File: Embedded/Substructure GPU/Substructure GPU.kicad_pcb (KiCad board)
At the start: 4 copper layers, 50 x 35 mm, 35 parts, among them J1 10171746-00021LF, J11 Substructure Power, J13 MicroSD, J2 HUB75 Right, J3 Display Power, J4 HUB75 Left, SW2 RST, U2 74HC245D_653, U3 74HC245D_653, U5 Substructure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

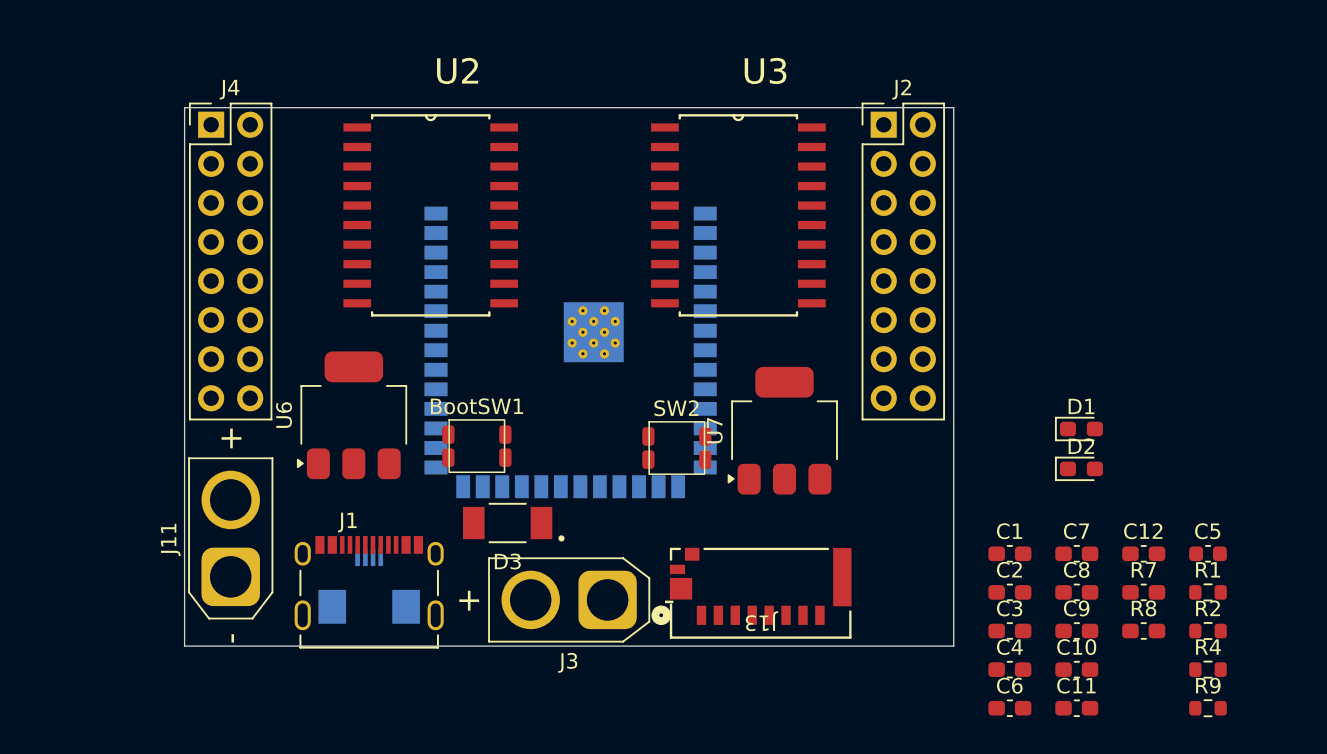
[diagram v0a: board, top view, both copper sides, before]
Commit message: Modified Board size
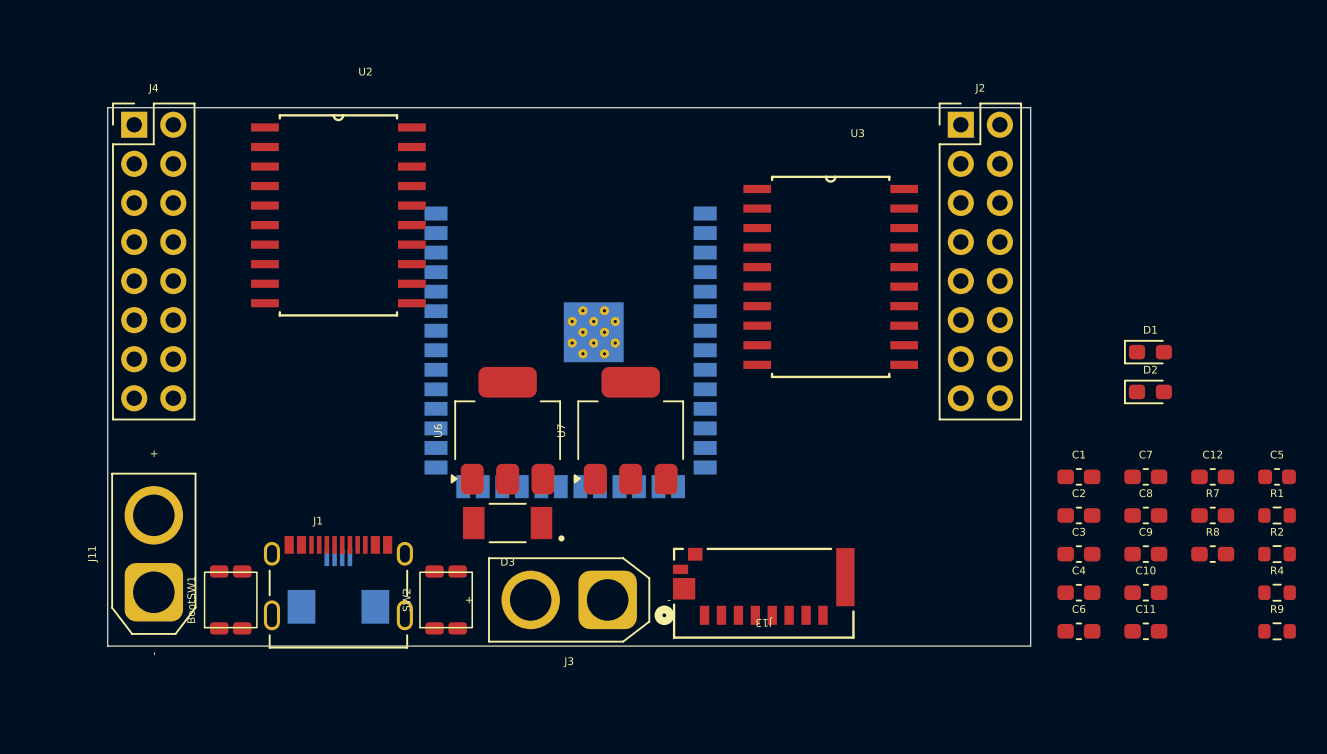
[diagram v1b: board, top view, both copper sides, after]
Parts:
- moved BootSW1 18.9 mm to (73.0, 72.0), turned to 90 degrees
- moved SW2 18.0 mm to (87.0, 72.0), turned to 90 degrees
- moved U6 10.0 mm to (91.0, 61.0)
- moved U7 10.0 mm to (99.0, 61.0)
- moved U3 7.21 mm to (112.0, 51.0)
- moved C10 6.72 mm to (132.5, 71.5)
- moved C11 6.72 mm to (132.5, 74.0)
- moved C12 6.72 mm to (136.8, 64.0)
- moved C5 6.72 mm to (141.0, 64.0)
- moved C7 6.72 mm to (132.5, 64.0)
- moved C8 6.72 mm to (132.5, 66.5)
- moved C9 6.72 mm to (132.5, 69.0)
- moved R1 6.72 mm to (141.0, 66.5)
- moved R2 6.72 mm to (141.0, 69.0)
- moved R4 6.72 mm to (141.0, 71.5)
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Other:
- board size 50 x 35 mm -> 60 x 35 mm

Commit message: Added Component placement for driver components
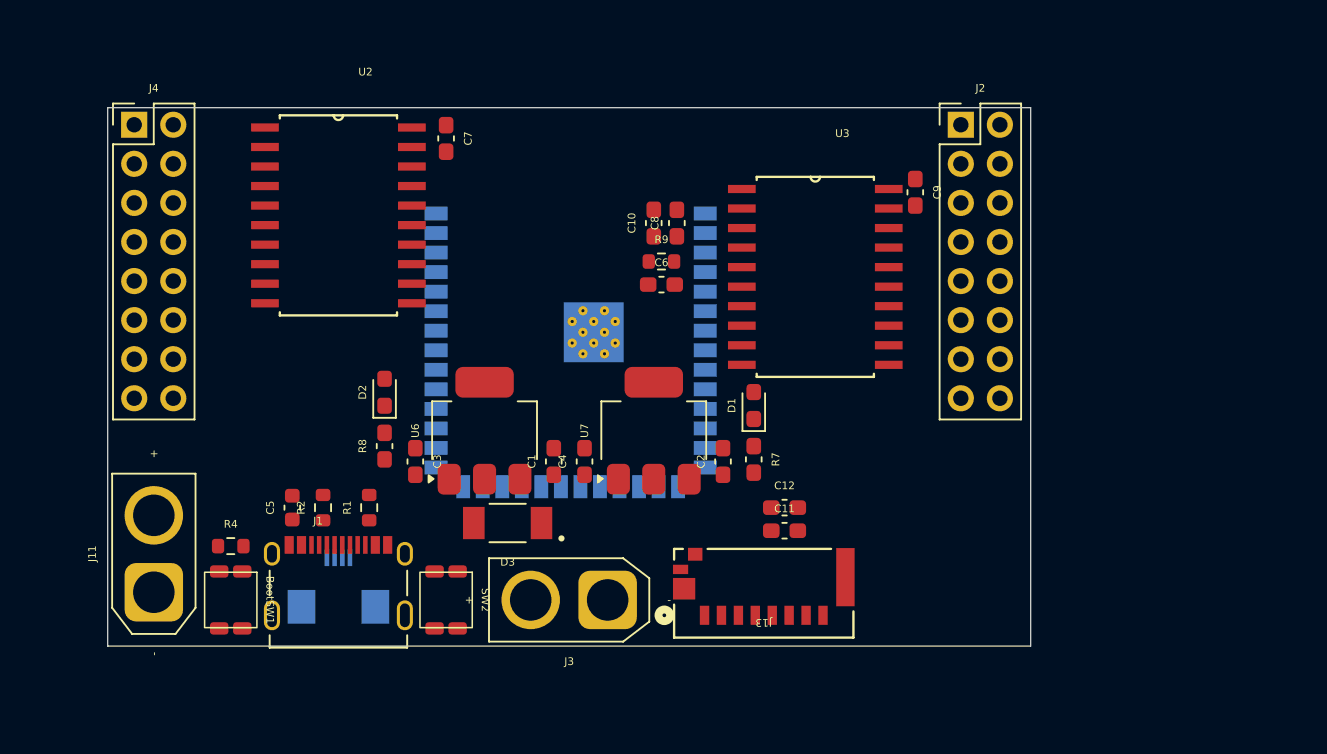
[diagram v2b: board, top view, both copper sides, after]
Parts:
- moved R4 68.1 mm to (73.0, 68.5)
- moved C5 64.0 mm to (77.0, 66.0), turned to 90 degrees
- moved R2 62.1 mm to (79.0, 66.0), turned to 90 degrees
- moved R1 59.0 mm to (82.0, 66.0), turned to 90 degrees
- moved R8 54.3 mm to (83.0, 62.0), turned to 90 degrees
- moved C7 50.5 mm to (87.0, 42.0), turned to -90 degrees
- moved D2 49.8 mm to (83.0, 58.5), turned to 90 degrees
- moved R9 46.7 mm to (101.0, 50.0)
- moved C3 43.6 mm to (85.0, 63.0), turned to -90 degrees
- moved C10 40.0 mm to (100.5, 47.5), turned to 90 degrees
- moved C8 35.9 mm to (102.0, 47.5), turned to 90 degrees
- moved C6 35.3 mm to (101.0, 51.5)
- moved C1 34.2 mm to (94.0, 63.0), turned to 90 degrees
- moved C4 33.3 mm to (96.0, 63.0), turned to 90 degrees
- moved R7 30.1 mm to (107.0, 62.9), turned to -90 degrees
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
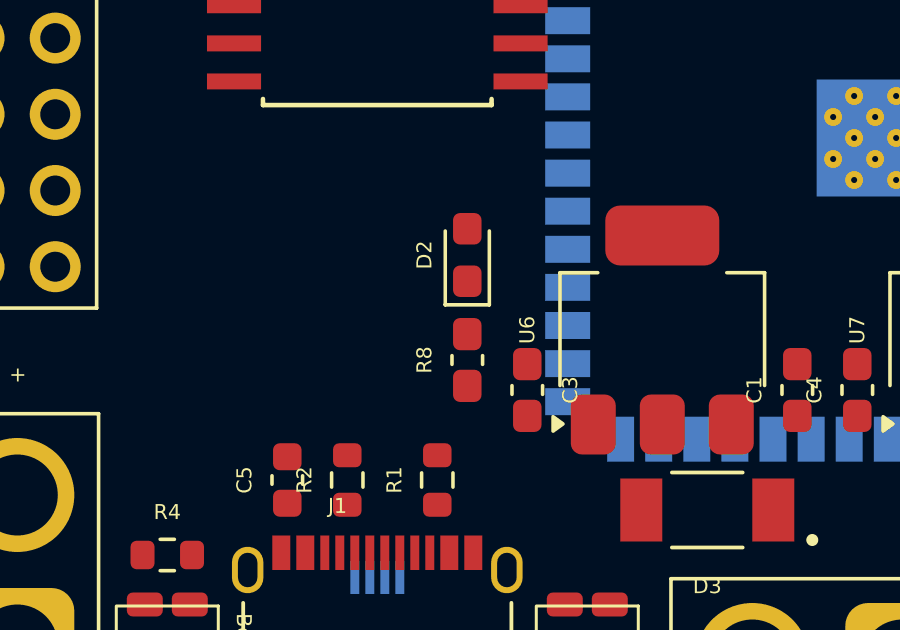
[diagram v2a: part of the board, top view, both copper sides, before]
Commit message: Added Pins to route in schematic
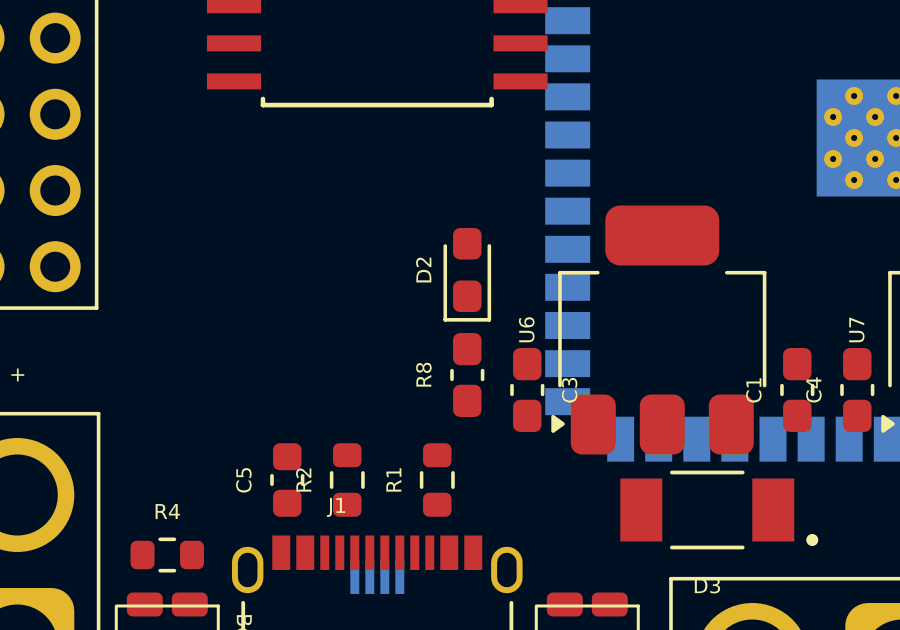
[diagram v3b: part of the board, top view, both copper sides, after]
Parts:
- moved D2 0.50 mm to (83.0, 59.0)
- moved R8 0.50 mm to (83.0, 62.5)
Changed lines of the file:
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@@
 	(footprint "Diode_SMD:D_0603_1608Metric_Pad1.05x0.95mm_HandSolder"
 		(layer "F.Cu")
-		(at 83 58.5 90)
+		(at 83 59 90)
 		(descr "Diode SMD 0603 (1608 Metric), square (rectangular) end terminal, IPC-7351 nominal, (Body size source: http://www.tortai-tech.com/upload/download/2011102023233369053.pdf), generated with kicad-footprint-generator")
 		(tags "diode handsolder")
@@
 	(footprint "Capacitor_SMD:C_0603_1608Metric_Pad1.08x0.95mm_HandSolder"
 		(layer "F.Cu")
-		(at 83 62 90)
+		(at 83 62.5 90)
 		(descr "Capacitor SMD 0603 (1608 Metric), square (rectangular) end terminal, IPC-7351 nominal with elongated pad for handsoldering. (Body size source: IPC-SM-782 page 76, https://www.pcb-3d.com/wordpress/wp-content/uploads/ipc-sm-782a_amendment_1_and_2.pdf), generated with kicad-footprint-generator")
 		(tags "capacitor handsolder")

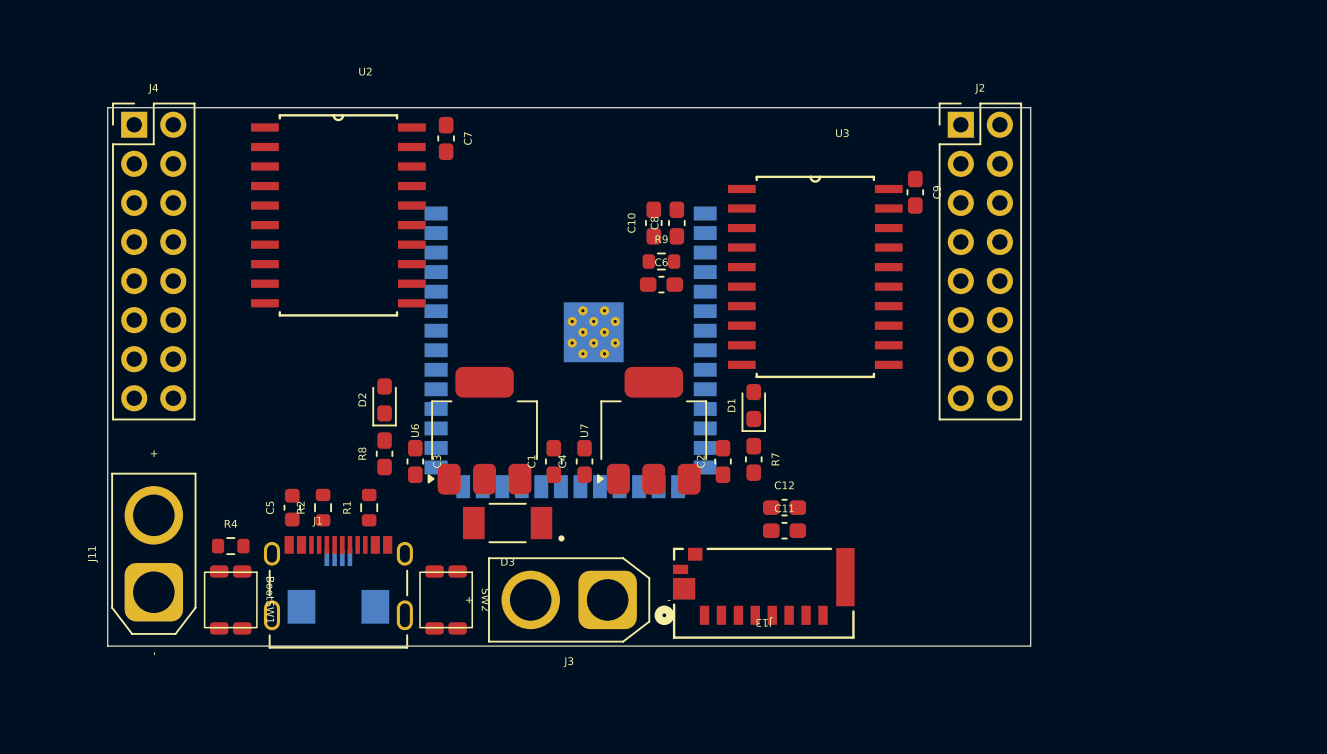
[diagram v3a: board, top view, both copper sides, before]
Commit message: Added GPU Routing
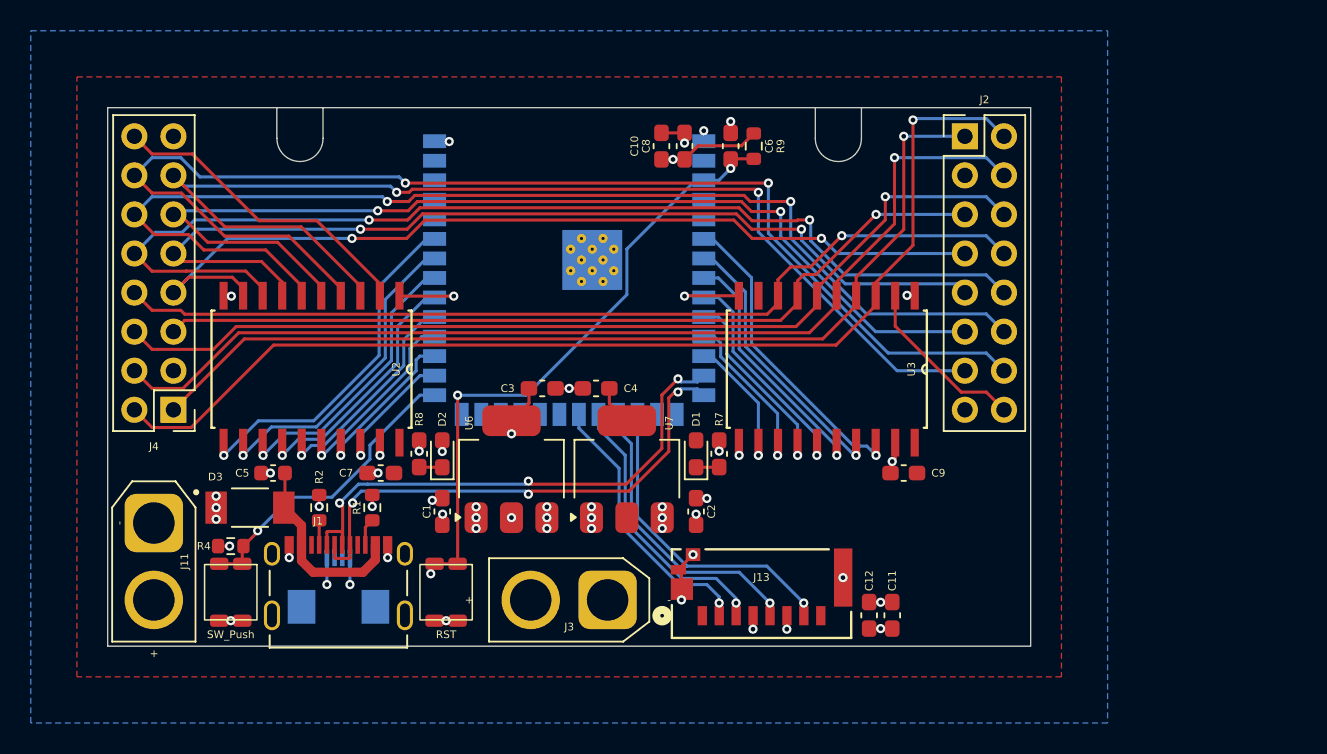
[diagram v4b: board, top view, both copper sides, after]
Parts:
- moved C7 22.2 mm to (82.8, 63.8), turned to 180 degrees
- moved J4 18.7 mm to (69.3, 59.6), turned to 180 degrees
- moved C9 18.3 mm to (116.8, 63.8), turned to 180 degrees
- moved D3 16.8 mm to (74.2, 66.0), turned to 0 degrees
- moved U2 10.2 mm to (78.2, 57.0), turned to -90 degrees
- moved C6 10.1 mm to (105.5, 42.5), turned to -90 degrees
- moved R9 9.60 mm to (107.0, 42.5), turned to -90 degrees
- moved C3 9.52 mm to (93.2, 58.2), turned to 0 degrees
- moved C11 8.90 mm to (116.0, 73.0), turned to 90 degrees
- moved C12 8.90 mm to (114.5, 73.0), turned to 90 degrees
- moved C1 7.95 mm to (86.8, 66.2), turned to -90 degrees
- moved U3 6.05 mm to (111.8, 57.0), turned to -90 degrees
- moved D2 5.13 mm to (86.8, 62.5)
- moved C10 5.02 mm to (101.0, 42.5)
- moved C8 5.02 mm to (102.5, 42.5)
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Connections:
- C1 pad 1: +5VS -> +RAWVS
- C2 pad 1: +5VS -> +RAWVS
- ESP1 pad 10: unconnected-(ESP1-GPIO17/U1TXD/ADC2_CH6-Pad10) -> Disp GPIO 12
- ESP1 pad 11: unconnected-(ESP1-GPIO18/U1RXD/ADC2_CH7/CLK_OUT3-Pad11) -> Disp GPIO 13
- ESP1 pad 12: unconnected-(ESP1-GPIO8/TOUCH8/ADC1_CH7/SUBSPICS1-Pad12) -> Disp GPIO 14
- ESP1 pad 17: unconnected-(ESP1-GPIO9/TOUCH9/ADC1_CH8/FSPIHD/SUBSPIHD-Pad17) -> SD SPI MISO
- ESP1 pad 18: unconnected-(ESP1-GPIO10/TOUCH10/ADC1_CH9/FSPICS0/FSPIIO4/SUBSPICS0-Pad18) -> SD SPI CLK
- ESP1 pad 19: unconnected-(ESP1-GPIO11/TOUCH11/ADC2_CH0/FSPID/FSPIIO5/SUBSPID-Pad19) -> SD SPI MOSI
- ESP1 pad 20: unconnected-(ESP1-GPIO12/TOUCH12/ADC2_CH1/FSPICLK/FSPIIO6/SUBSPICLK-Pad20) -> SD SPI CS
- ESP1 pad 28: unconnected-(ESP1-SPIIO6/GPIO35/FSPID/SUBSPID-Pad28) -> Disp GPIO 0
- ESP1 pad 29: unconnected-(ESP1-SPIIO7/GPIO36/FSPICLK/SUBSPICLK-Pad29) -> Disp GPIO 1
- ESP1 pad 30: unconnected-(ESP1-SPIDQS/GPIO37/FSPIQ/SUBSPIQ-Pad30) -> Disp GPIO 2
- ESP1 pad 31: unconnected-(ESP1-GPIO38/FSPIWP/SUBSPIWP-Pad31) -> Disp GPIO 3
- ESP1 pad 32: unconnected-(ESP1-MTCK/GPIO39/CLK_OUT3/SUBSPICS1-Pad32) -> Disp GPIO 4
- ESP1 pad 33: unconnected-(ESP1-MTDO/GPIO40/CLK_OUT2-Pad33) -> Disp GPIO 5
- ESP1 pad 34: unconnected-(ESP1-MTDI/GPIO41/CLK_OUT1-Pad34) -> Disp GPIO 6
- ESP1 pad 35: unconnected-(ESP1-MTMS/GPIO42-Pad35) -> Disp GPIO 7
- ESP1 pad 6: unconnected-(ESP1-GPIO6/TOUCH6/ADC1_CH5-Pad6) -> Disp GPIO 8
- ESP1 pad 7: unconnected-(ESP1-GPIO7/TOUCH7/ADC1_CH6-Pad7) -> Disp GPIO 9
- ESP1 pad 8: unconnected-(ESP1-GPIO15/U0RTS/ADC2_CH4/XTAL_32K_P-Pad8) -> Disp GPIO 10
- ESP1 pad 9: unconnected-(ESP1-GPIO16/U0CTS/ADC2_CH5/XTAL_32K_N-Pad9) -> Disp GPIO 11
- J2 pad 16: OE -> OE1
- J4 pad 16: OE -> OE0
- U2 pad 11: unconnected-(U2-B7-Pad11) -> Disp GPIO 7
- U2 pad 12: unconnected-(U2-B6-Pad12) -> Disp GPIO 6
- U2 pad 13: unconnected-(U2-B5-Pad13) -> Disp GPIO 5
- U2 pad 14: unconnected-(U2-B4-Pad14) -> Disp GPIO 4
- U2 pad 15: unconnected-(U2-B3-Pad15) -> Disp GPIO 3
- U2 pad 16: unconnected-(U2-B2-Pad16) -> Disp GPIO 2
- U2 pad 17: unconnected-(U2-B1-Pad17) -> Disp GPIO 1
- U2 pad 18: unconnected-(U2-B0-Pad18) -> Disp GPIO 0
- U2 pad 2: OE -> OE0
- U2 pad 3: G0 -> LAT
- U2 pad 4: R0 -> CLK
- U2 pad 5: B0 -> D
- U2 pad 6: G1 -> C
- U2 pad 7: R1 -> B
- U2 pad 8: E -> A
- U2 pad 9: B1 -> E
- U3 pad 12: unconnected-(U3-B6-Pad12) -> Disp GPIO 14
- U3 pad 13: unconnected-(U3-B5-Pad13) -> Disp GPIO 13
- U3 pad 14: unconnected-(U3-B4-Pad14) -> Disp GPIO 12
- U3 pad 15: unconnected-(U3-B3-Pad15) -> Disp GPIO 11
- U3 pad 16: unconnected-(U3-B2-Pad16) -> Disp GPIO 10
- U3 pad 17: unconnected-(U3-B1-Pad17) -> Disp GPIO 9
- U3 pad 18: unconnected-(U3-B0-Pad18) -> Disp GPIO 8
- U3 pad 2: A -> OE1
- U3 pad 3: B -> R0
- U3 pad 4: C -> G0
- U3 pad 5: D -> B0
- U3 pad 6: CLK -> R1
- U3 pad 7: LAT -> G1
- U3 pad 8: unconnected-(U3-A6-Pad8) -> B1
- U6 pad 3: +5VS -> +RAWVS
- U7 pad 3: +5VS -> +RAWVS
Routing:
- net CLK: track 0.00 -> 81.6 mm, vias 0 -> 2
- net C: track 0.00 -> 75.8 mm, vias 0 -> 2
- net LAT: track 0.00 -> 74.2 mm, vias 0 -> 2
- net R0: track 0.00 -> 71.4 mm, vias 0 -> 1
- net A: track 0.00 -> 70.6 mm, vias 0 -> 2
- net D: track 0.00 -> 68.4 mm, vias 0 -> 2
- net B0: track 0.00 -> 67.1 mm, vias 0 -> 1
- net B: track 0.00 -> 63.8 mm, vias 0 -> 2
- net G0: track 0.00 -> 63.4 mm, vias 0 -> 1
- net R1: track 0.00 -> 63.1 mm, vias 0 -> 1
- net B1: track 0.00 -> 60.6 mm, vias 0 -> 1
- net E: track 0.00 -> 60.0 mm, vias 0 -> 2
- net G1: track 0.00 -> 55.5 mm, vias 0 -> 1
- net +RAWVS: track 0.00 -> 54.5 mm, vias 0 -> 11
- net GND: track 0.00 -> 42.2 mm, vias 0 -> 36
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- added copper zone on B.Cu, net +3V3
- added copper zone on F.Cu, net +5V
- added copper zone on In1.Cu, net GND
- added copper zone on In2.Cu, net GND
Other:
- outline, holes or cut-outs redrawn
